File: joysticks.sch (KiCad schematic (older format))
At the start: 44 parts, among them CN4 JOY1, CN5 JOY2, U11 74LS125, U17 74LS244, U18 74LS244, U93 DT1042, U94 DT1042, U95 DT1042

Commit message: Add resistor pack type
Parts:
- RP5: Notes (none) -> Bussed
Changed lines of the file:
@@
 F 2 "Resistor_THT:R_Array_SIP6" V 6105 4095 50  0001 C CNN
 F 3 "http://www.vishay.com/docs/31509/csc.pdf" H 5730 4095 50  0001 C CNN
+F 4 "Bussed" H 5730 4095 50  0001 C CNN "Notes"
 	1    5730 4095
 	1    0    0    -1

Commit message: Connect SID audio output
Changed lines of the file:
@@
 Wire Wire Line
 	4050 6965 3880 6965
-Text Label 4820 2650 0    50   ~ 0
-f1d
 Text Label 5445 6970 0    50   ~ 0
 f2d

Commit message: Well yeah maybe
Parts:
- removed JP1: JOY2_SELECT, LittleSixteen:SolderJumper2x, symbol Jumper:Jumper_3_Bridged12
- removed JP2: JOY1_SELECT, LittleSixteen:SolderJumper2x, symbol Jumper:Jumper_3_Bridged12
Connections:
- net d1: now also U11.5
- net d2: now also U11.2
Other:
- note removed: "The JP1 and JP2 jumpers are not present\nin the original schematics but I have traced\nthem on my board. They are labeled "D1" and\n"D2", I have renamed them to avoid conflicts\nwith the diodes bearing the same labels.\n\nTheir purpose seems to be able to enable the\njoysticks after passing through the keyboard\ndriver. Since it seems the latter was introduced\nlate in the x264 architecture, mayb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"
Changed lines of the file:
@@
 Wire Wire Line
 	2955 5730 2955 5805
-Text Label 1660 5030 0    50   ~ 0
+Text Label 1660 5480 0    50   ~ 0
 d1
-Wire Wire Line
-	2540 5480 2655 5480
 $Comp
 L 74xx:74LS125 U11
@@
 	1    0    0    -1
 $EndComp
-Text GLabel 1230 2255 0    50   Input ~ 0
+Text GLabel 1230 2705 0    50   Input ~ 0
 d[0..7]
 Wire Bus Line
-	1230 2255 1560 2255
+	1230 2705 1560 2705
 Entry Wire Line
-	1560 4930 1660 5030
+	1560 5380 1660 5480
 Entry Wire Line
-	1560 2255 1660 2355
+	1560 2705 1660 2805
 $Comp
 L 74xx:74LS125 U11
@@
 	1    0    0    -1
 $EndComp
-Text Label 1660 2355 0    50   ~ 0
+Text Label 1660 2805 0    50   ~ 0
 d2
 Wire Wire Line
@@
 Text Notes 5875 2680 2    50   ~ 0
 The (apparently)\nodd connections\nhere are to\nsimplify routing!
-$Comp
-L Jumper:Jumper_3_Bridged12 JP1
-U 1 1 61F59301
-P 2390 5480
-F 0 "JP1" V 2344 5547 50  0000 L CNN
-F 1 "JOY2_SELECT" V 2435 5547 50  0000 L CNN
-F 2 "LittleSixteen:SolderJumper2x" H 2390 5480 50  0001 C CNN
-F 3 "~" H 2390 5480 50  0001 C CNN
-	1    2390 5480
-	0    -1   1    0
-$EndComp
-Wire Wire Line
-	2390 5730 2390 5920
-Wire Wire Line
-	2390 5920 2160 5920
-Text GLabel 2160 5920 0    50   Input ~ 0
-D1_LATCHED
-Wire Wire Line
-	2540 2805 2655 2805
-$Comp
-L Jumper:Jumper_3_Bridged12 JP2
-U 1 1 61F9FE8A
-P 2390 2805
-F 0 "JP2" V 2344 2872 50  0000 L CNN
-F 1 "JOY1_SELECT" V 2435 2872 50  0000 L CNN
-F 2 "LittleSixteen:SolderJumper2x" H 2390 2805 50  0001 C CNN
-F 3 "~" H 2390 2805 50  0001 C CNN
-	1    2390 2805
-	0    -1   1    0
-$EndComp
-Wire Wire Line
-	2390 3055 2390 3245
-Wire Wire Line
-	2390 3245 2160 3245
-Text GLabel 2160 3245 0    50   Input ~ 0
-D2_LATCHED
-Wire Wire Line
-	2390 2355 2390 2555
-Wire Wire Line
-	1660 2355 2390 2355
-Wire Wire Line
-	2390 5030 2390 5230
-Wire Wire Line
-	1660 5030 2390 5030
 Wire Wire Line
 	5930 1480 5930 1805
@@
 	8660 4775 8905 4780
 Wire Bus Line
-	1560 2255 1560 4930
-Text Notes 2575 4575 2    50   ~ 0
-The JP1 and JP2 jumpers are not present\nin the original schematics but I have traced\nthem on my board. They are labeled "D1" and\n"D2", I have renamed them to avoid conflicts\nwith the diodes bearing the same labels.\n\nTheir purpose seems to be able to enable the\njoysticks after passing through the keyboard\ndriver. Since it seems  the latter was introduced\nlate in the x264 architecture, maybe the\ndesigners weren't sure what was best and kept\nboth possibilities.
+	1560 2705 1560 5380
 NoConn ~ 7200 4880
 Wire Wire Line
@@
 	0    -1   -1   0
 $EndComp
+Wire Wire Line
+	1660 2805 2655 2805
+Wire Wire Line
+	1660 5480 2655 5480
 Wire Bus Line
 	9685 1705 9685 4385

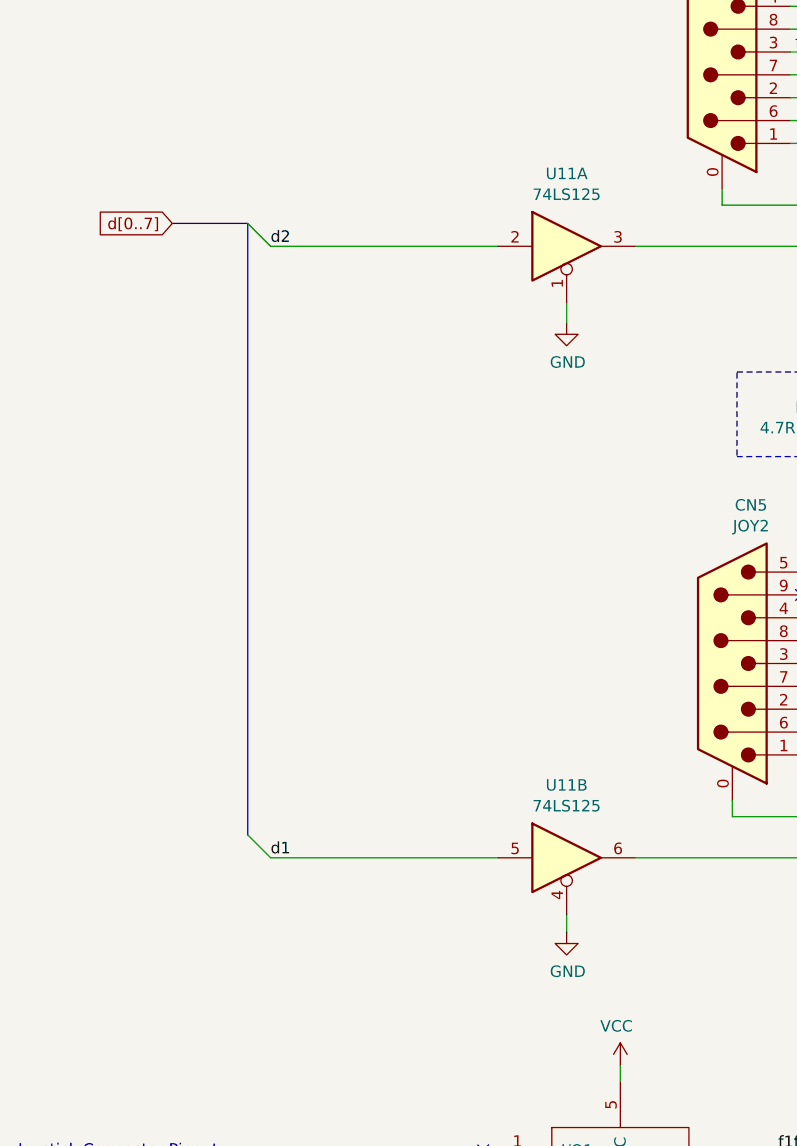
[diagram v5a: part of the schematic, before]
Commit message: Add 512kB RAM expansions, Hannes-style
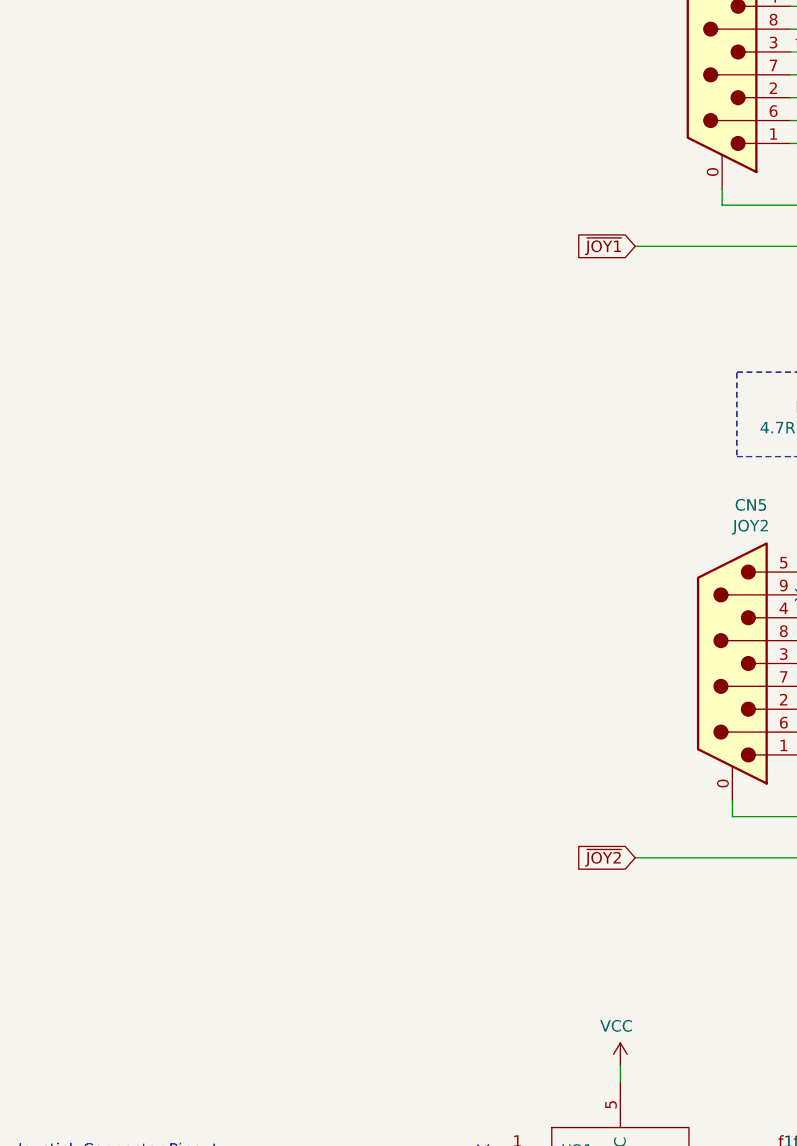
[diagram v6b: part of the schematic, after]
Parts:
- removed U11: 74LS125, LittleSixteen:DIP-14_W7.62mm_Socket_LongPads, symbol 74xx:74LS125
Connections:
- net ~JOY1: now reaches U17.1 (1OE), U17.19 (2OE)
- net ~JOY2: now reaches U18.1 (1OE), U18.19 (2OE)
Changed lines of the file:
@@
-	1    0    0    -1
-$EndComp
-$Comp
-L power:GND #PWR0107
-U 1 1 5DFEE778
-P 2955 3140
-F 0 "#PWR0107" H 2955 2890 50  0001 C CNN
-F 1 "GND" H 2960 2967 50  0000 C CNN
-F 2 "" H 2955 3140 50  0001 C CNN
-F 3 "" H 2955 3140 50  0001 C CNN
-	1    2955 3140
 	1    0    0    -1
 $EndComp
 Wire Wire Line
 	3255 5480 6060 5480
-Wire Wire Line
-	2955 3055 2955 3140
-Wire Wire Line
-	2955 5730 2955 5805
-Text Label 1660 5480 0    50   ~ 0
-d1
-$Comp
-L 74xx:74LS125 U11
-U 2 1 5E227156
-P 2955 5480
-F 0 "U11" H 2955 5797 50  0000 C CNN
-F 1 "74LS125" H 2955 5706 50  0000 C CNN
-F 2 "LittleSixteen:DIP-14_W7.62mm_Socket_LongPads" H 2955 5480 50  0001 C CNN
-F 3 "http://www.ti.com/lit/gpn/sn74LS125" H 2955 5480 50  0001 C CNN
-	2    2955 5480
-	1    0    0    -1
-$EndComp
-$Comp
-L power:GND #PWR0110
-U 1 1 5E19A809
-P 2955 5805
-F 0 "#PWR0110" H 2955 5555 50  0001 C CNN
-F 1 "GND" H 2960 5632 50  0000 C CNN
-F 2 "" H 2955 5805 50  0001 C CNN
-F 3 "" H 2955 5805 50  0001 C CNN
-	1    2955 5805
-	1    0    0    -1
-$EndComp
-Text GLabel 1230 2705 0    50   Input ~ 0
-d[0..7]
-Wire Bus Line
-	1230 2705 1560 2705
-Entry Wire Line
-	1560 5380 1660 5480
-Entry Wire Line
-	1560 2705 1660 2805
-$Comp
-L 74xx:74LS125 U11
-U 1 1 5DFC8E43
-P 2955 2805
-F 0 "U11" H 2955 3122 50  0000 C CNN
-F 1 "74LS125" H 2955 3031 50  0000 C CNN
-F 2 "LittleSixteen:DIP-14_W7.62mm_Socket_LongPads" H 2955 2805 50  0001 C CNN
-F 3 "http://www.ti.com/lit/gpn/sn74LS125" H 2955 2805 50  0001 C CNN
-	1    2955 2805
-	1    0    0    -1
-$EndComp
-Text Label 1660 2805 0    50   ~ 0
-d2
 Wire Wire Line
 	6200 5380 6060 5380
@@
 Wire Wire Line
 	8660 4775 8905 4780
-Wire Bus Line
-	1560 2705 1560 5380
 NoConn ~ 7200 4880
 Wire Wire Line
@@
 	0    -1   -1   0
 $EndComp
-Wire Wire Line
-	1660 2805 2655 2805
-Wire Wire Line
-	1660 5480 2655 5480
 Wire Bus Line
 	9685 1705 9685 4385
+Text GLabel 3255 2805 0    50   Input ~ 0
+~JOY1
+Text GLabel 3255 5480 0    50   Input ~ 0
+~JOY2
 $EndSCHEMATC

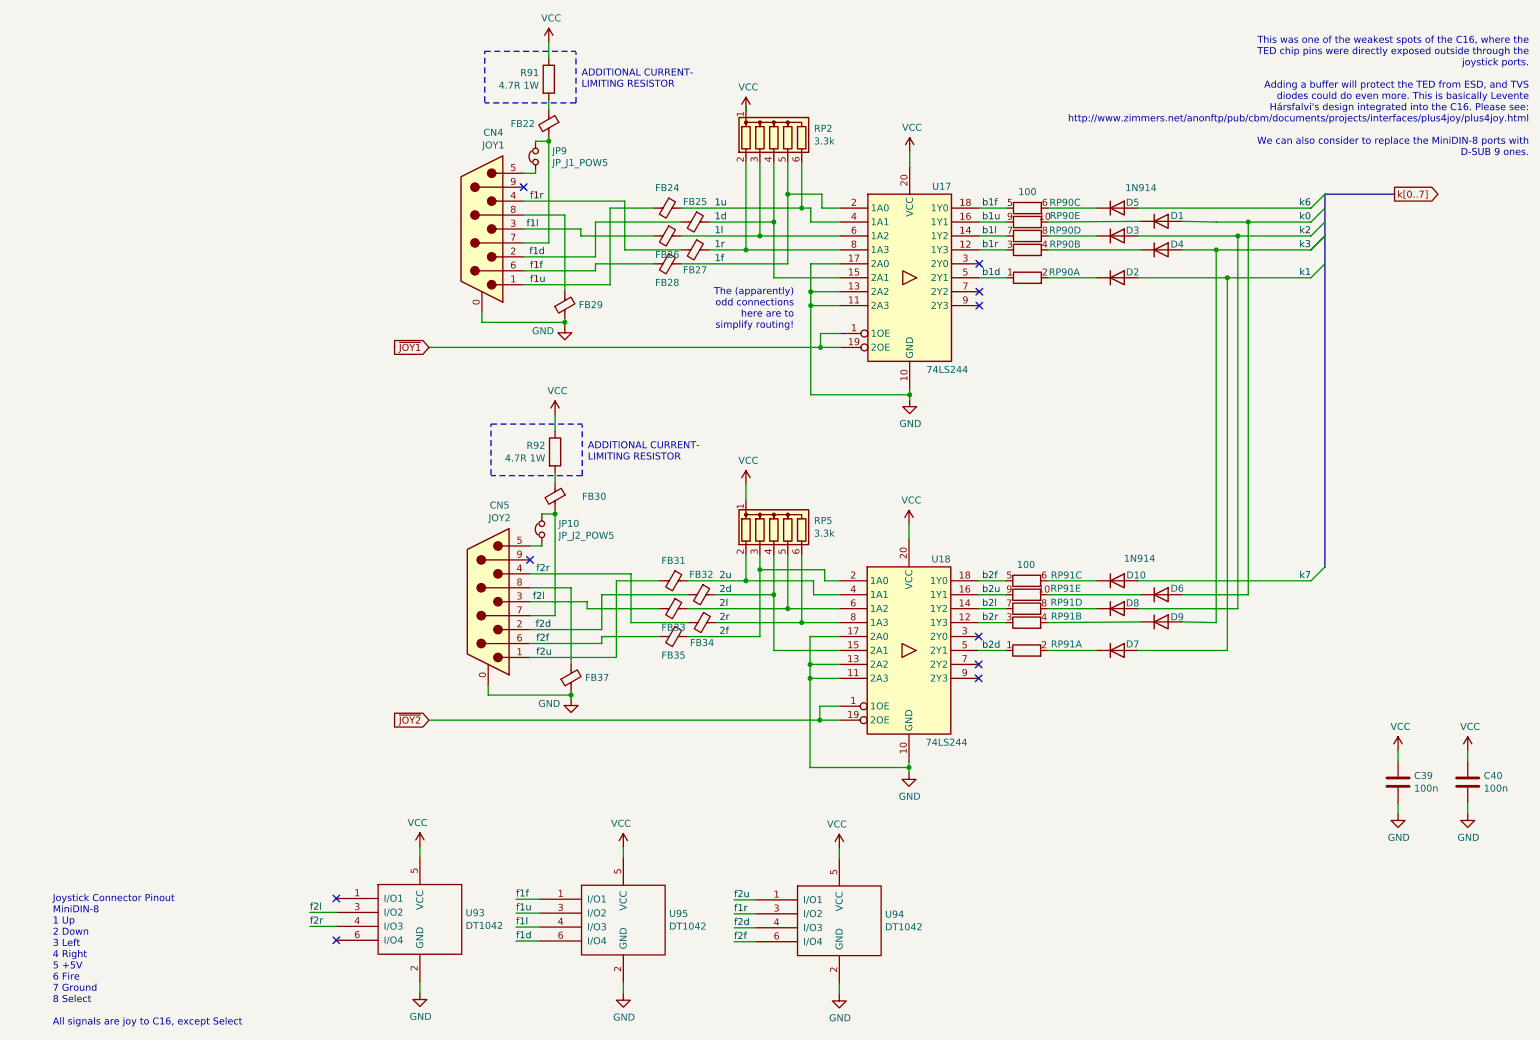
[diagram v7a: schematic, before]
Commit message: Replace joystick buffers with '245s This was done for economy of scale, as we already have other '245s onboard
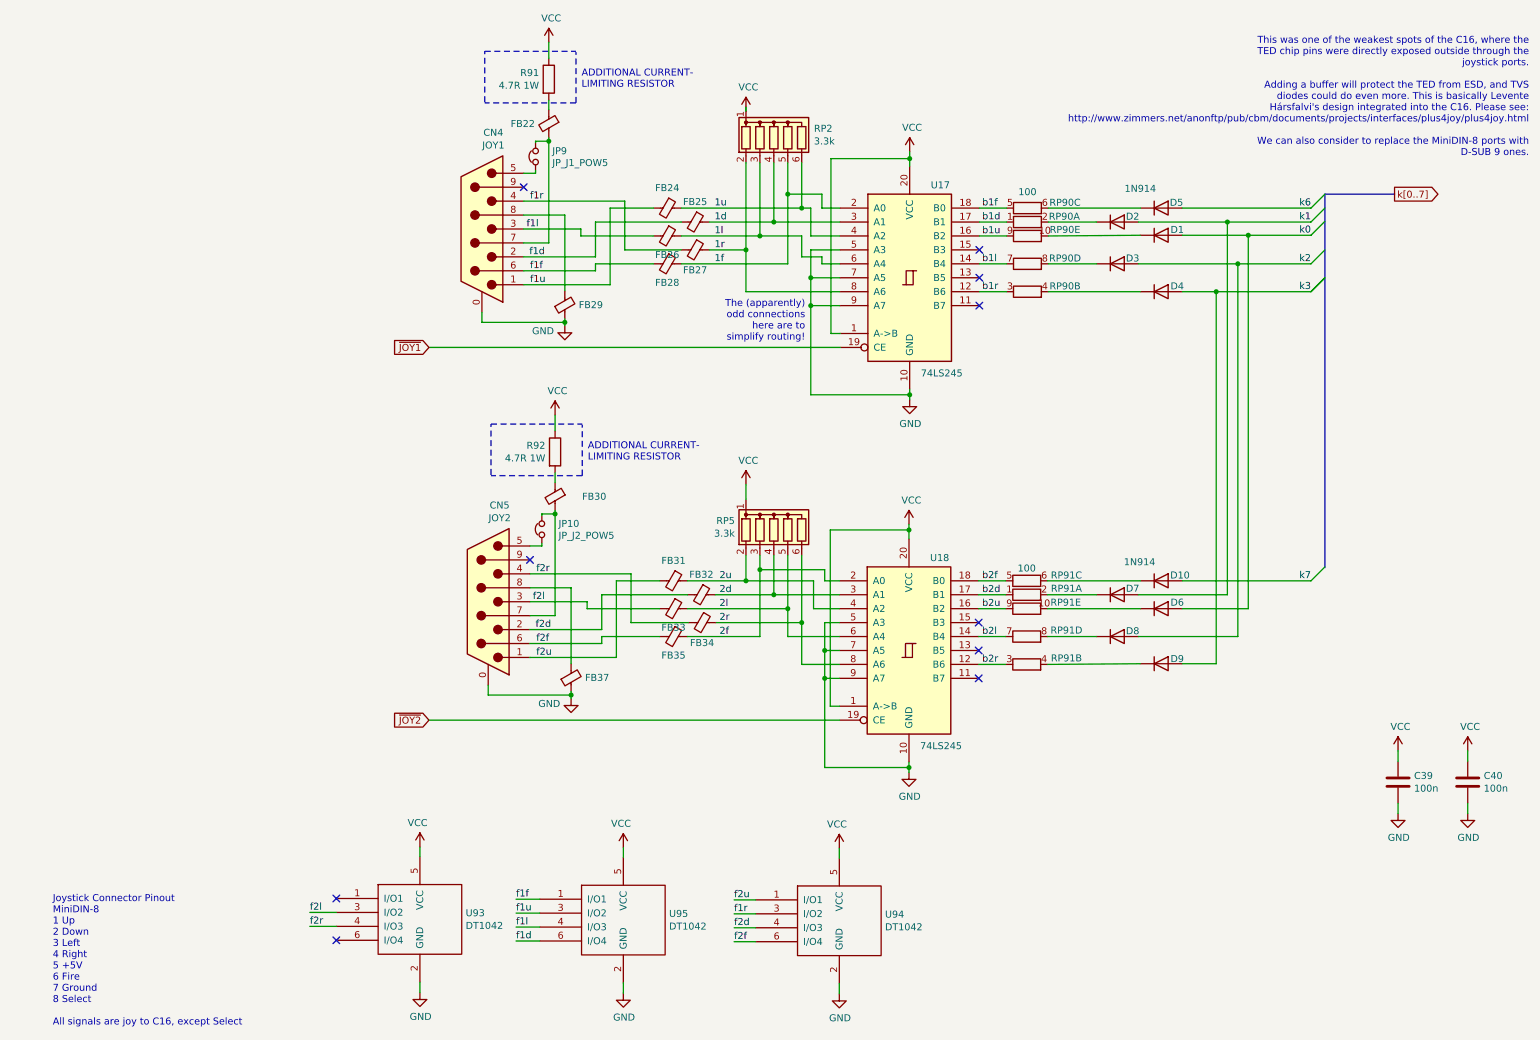
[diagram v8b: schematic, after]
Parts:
- removed U17, U18: 74LS244, LittleSixteen:DIP-20_W7.62mm_Socket_LongPads, symbol 74xx:74AHCT244
- added U17, U18: 74LS245, LittleSixteen:DIP-20_W7.62mm_Socket_LongPads, symbol 74xx:74LS245
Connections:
- net 1d: now also U17.3 (A1)
- net 1f: now also U17.2 (A0)
- net 1l: now also U17.6 (A4)
- net 1r: now also U17.8 (A6)
- net 1u: now also U17.4 (A2)
- net 2d: now also U18.3 (A1)
- net 2f: now also U18.2 (A0)
- net 2l: now also U18.6 (A4)
- net 2r: now also U18.8 (A6)
- net 2u: now also U18.4 (A2)
- net GND: now also U17.10 (GND), U17.5 (A3), U17.7 (A5), U17.9 (A7), U18.10 (GND), U18.5 (A3), U18.7 (A5), U18.9 (A7)
- net VCC: now also U17.1 (A->B), U17.20 (VCC), U18.1 (A->B), U18.20 (VCC)
- net b1d: now also U17.17 (B1)
- net b1f: now also U17.18 (B0)
- net b1l: now also U17.14 (B4)
- net b1r: now also U17.12 (B6)
- net b1u: now also U17.16 (B2)
- net b2d: now also U18.17 (B1)
- net b2f: now also U18.18 (B0)
- net b2l: now also U18.14 (B4)
- net b2r: now also U18.12 (B6)
- net b2u: now also U18.16 (B2)
- net ~JOY1: now also U17.19 (CE)
- net ~JOY2: now also U18.19 (CE)
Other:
- moved on the sheet: D1, D10, D2, D3, D4, D5, D6, D7, D8, D9, RP90A, RP90B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
